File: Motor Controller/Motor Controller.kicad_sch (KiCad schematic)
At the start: 5 parts, among them J1 Conn_01x03_Pin, U1 SN74LV1T34DBV

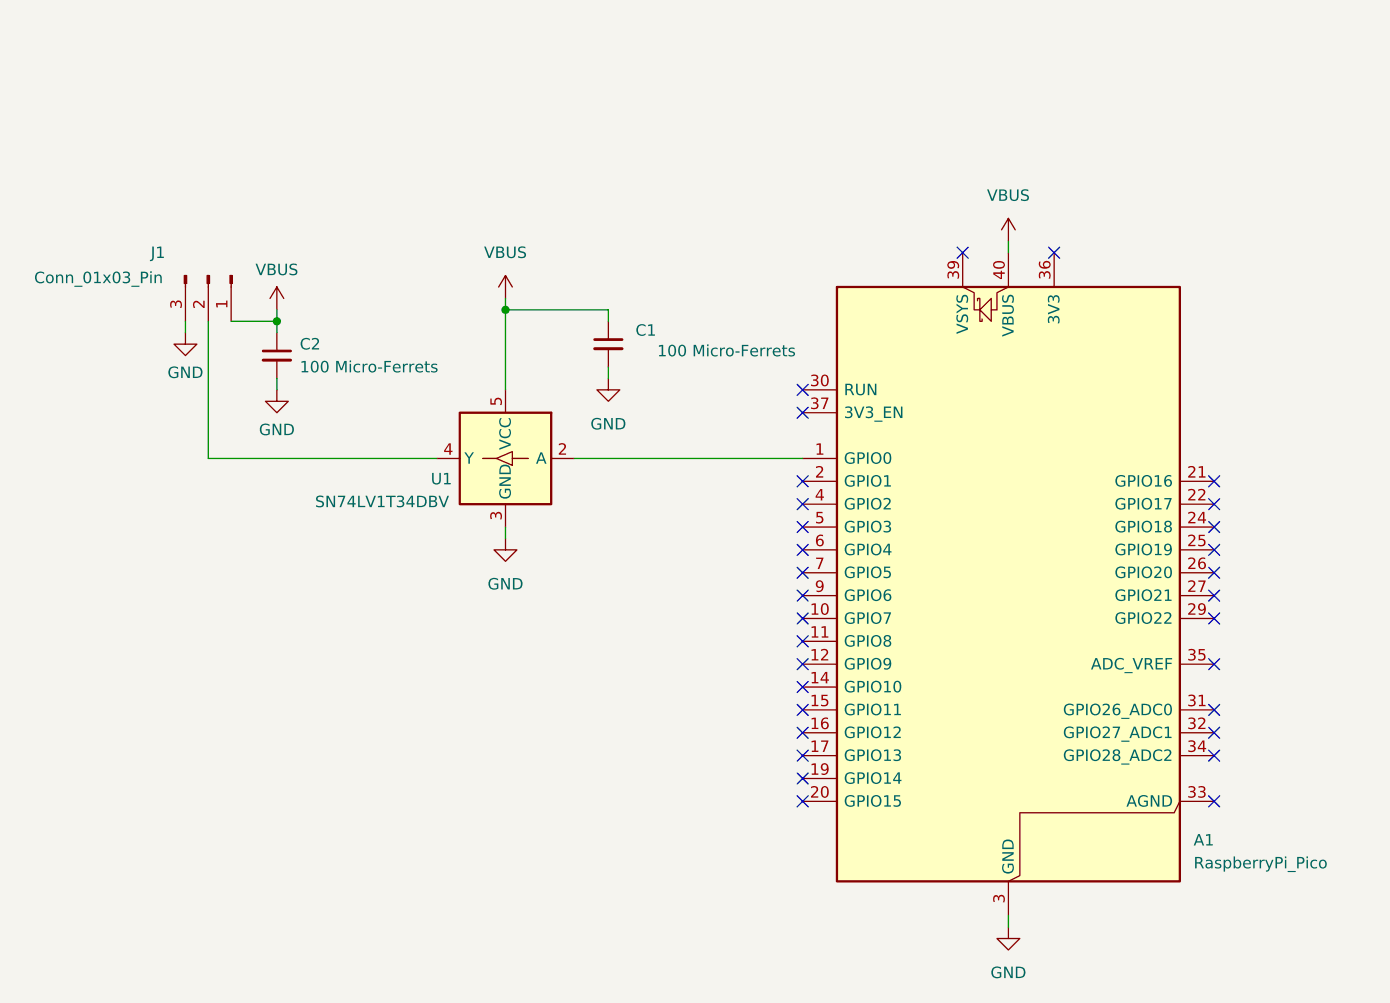
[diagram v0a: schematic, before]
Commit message: Replaced with revision 2 and made some small fixes; ready for export
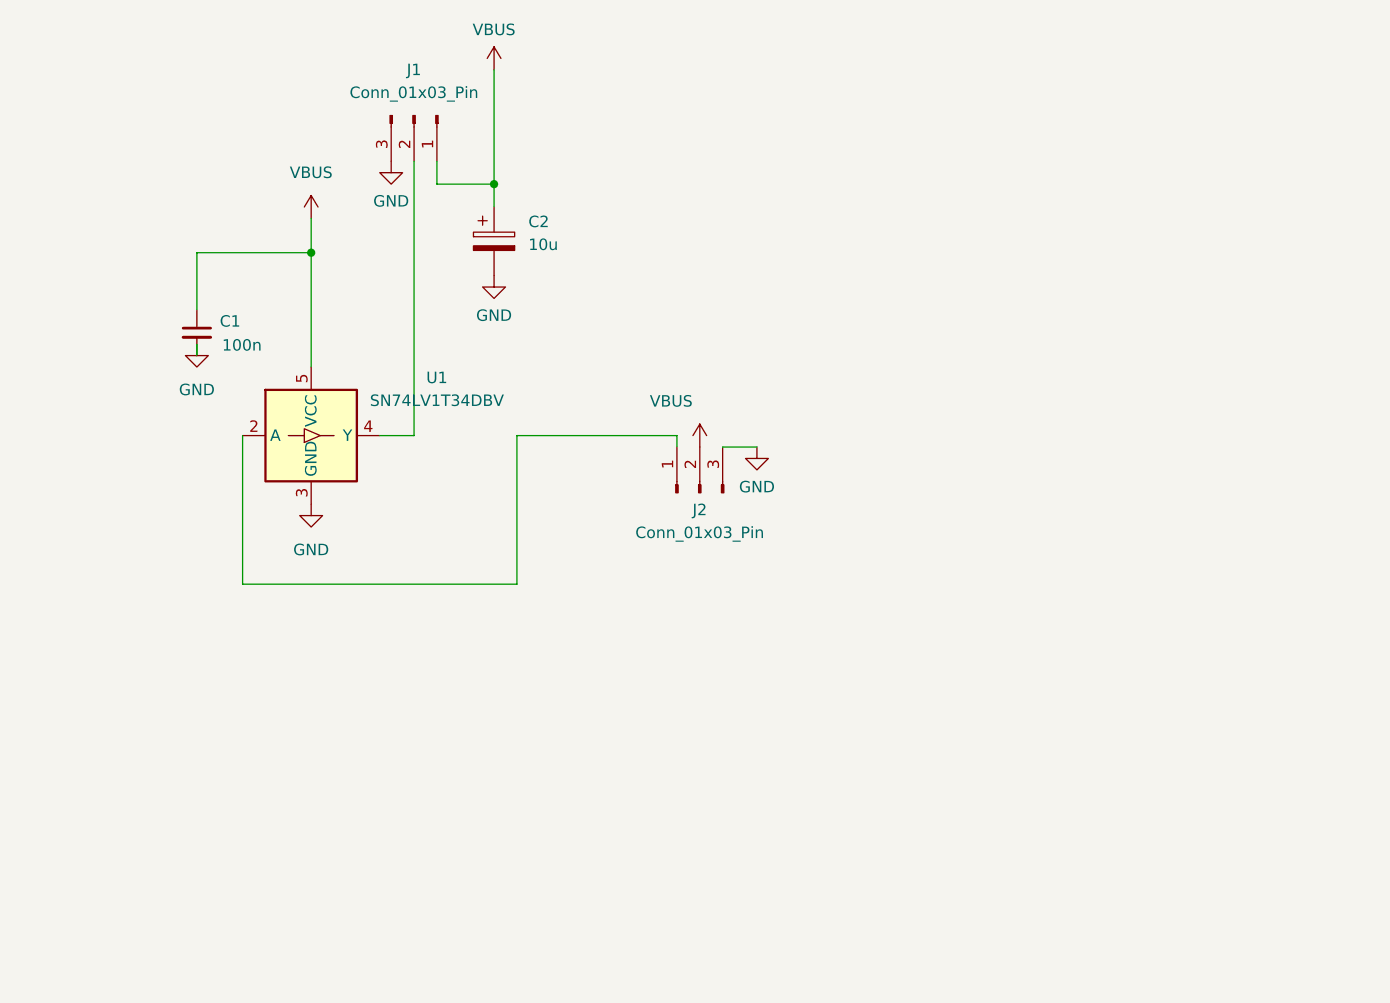
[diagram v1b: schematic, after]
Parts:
- removed A1: RaspberryPi_Pico, Module:RaspberryPi_Pico_Common_Unspecified, symbol MCU_Module:RaspberryPi_Pico
- removed C2: 100 Micro-Ferrets, Capacitor_THT:CP_Radial_D5.0mm_P2.00mm, symbol Device:C_Small
- added C2: 10u, Capacitor_THT:CP_Radial_D5.0mm_P2.00mm, symbol Device:C_Polarized
- added J2: Conn_01x03_Pin, Connector_PinHeader_2.54mm:PinHeader_1x03_P2.54mm_Vertical, symbol Connector:Conn_01x03_Pin
- C1: value 100 Micro-Ferrets -> 100n
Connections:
- net GND: now also C2.2, J2.3 (Pin_3)
- net VBUS: now also C2.1, J2.2 (Pin_2)
- net at U1.2 (A): now also J2.1 (Pin_1)
- no-connect marks 31 -> 0
